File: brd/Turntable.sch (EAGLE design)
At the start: 117 parts, among them CON1 Pannel, CON2 CAN, CON3 Turntable, CON4 STEPPER_CON, CON5 STEPPER_CON, CON8 SPK, IC1 7805, IC2 LM393N, J1 MiniStp2, J10 MiniStp1, Q1 BS170, SW1 EC12E_SW, U2 LED NANO, X1 AK500/2+M, X2 AK500/2+M, X3 MAB 5SH Conrad: 738247 - VQ, X4 AK500/2+M, X5 Reichelt MEBP 8-8S

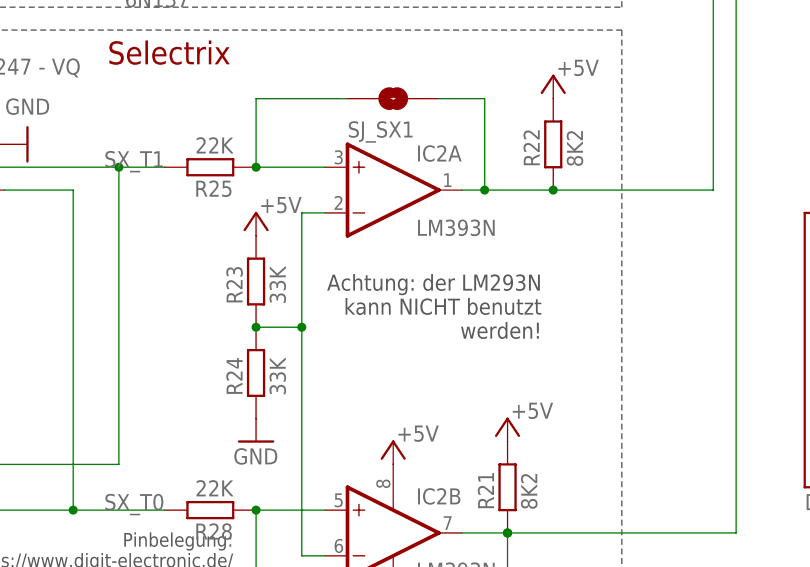
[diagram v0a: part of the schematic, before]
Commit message: Updated LM292 Text
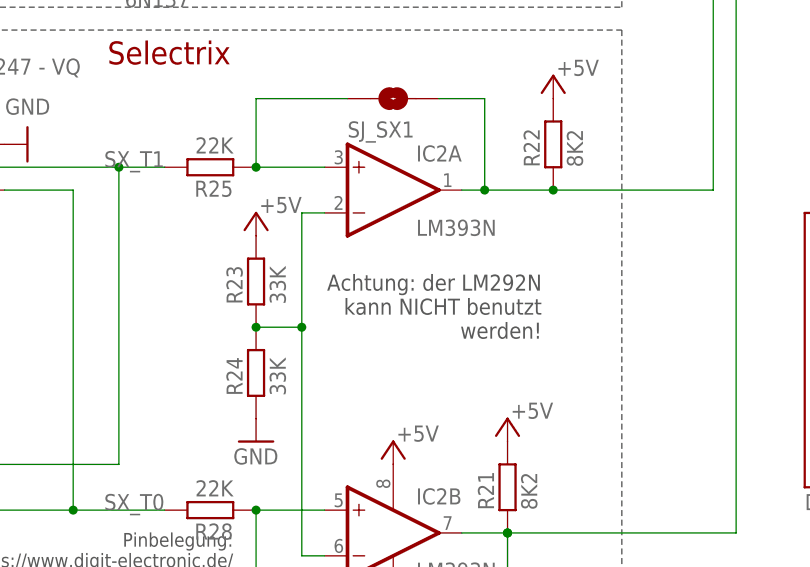
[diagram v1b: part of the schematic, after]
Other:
- note added: "Achtung: der LM292N kann NICHT benutzt werden!"
- note removed: "Achtung: der LM293N kann NICHT benutzt werden!"
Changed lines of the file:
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@@
 <wire x1="6.35" y1="78.74" x2="116.84" y2="78.74" width="0.1524" layer="97" style="shortdash"/>
 <wire x1="116.84" y1="78.74" x2="116.84" y2="6.35" width="0.1524" layer="97" style="shortdash"/>
-<text x="107.95" y="44.45" size="1.778" layer="97" rot="MR0">Achtung: der LM293N
+<text x="107.95" y="44.45" size="1.778" layer="97" rot="MR0">Achtung: der LM292N
 kann NICHT benutzt
 werden!</text>
